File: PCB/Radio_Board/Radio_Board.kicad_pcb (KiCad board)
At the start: 2 copper layers, 1 part, among them J1 Conn_02x08_Counter_Clockwise

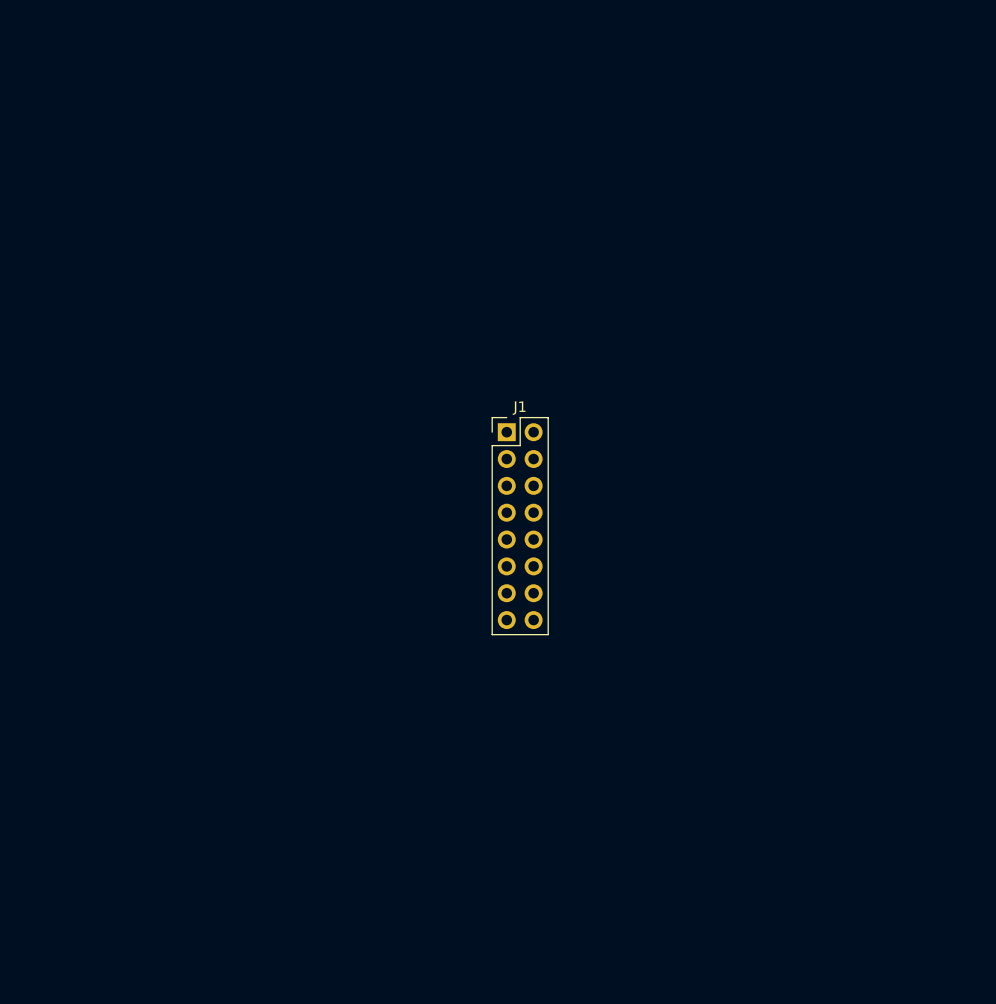
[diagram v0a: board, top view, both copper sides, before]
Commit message: added connector and started layout
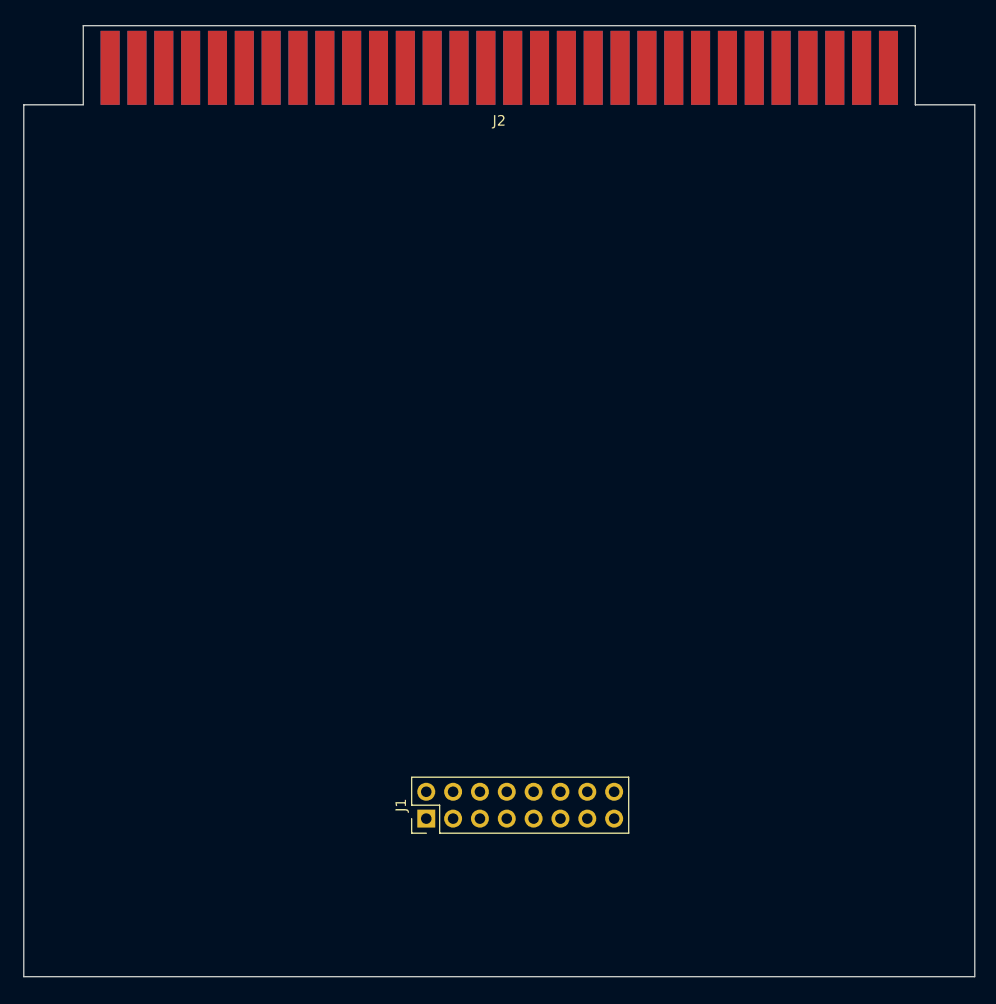
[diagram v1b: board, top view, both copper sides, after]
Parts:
- added J2: SE2-30, SE2-30:SE2-30, F.Cu at (148.8, 56.2)
- moved J1 37.4 mm to (141.8, 127.3), turned to 90 degrees
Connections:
- net /+5V renamed +5V
- net /GND renamed GND
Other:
- board outline added: 90 x 90 mm

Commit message: Wired Layout
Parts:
- removed J1: Conn_02x08_Counter_Clockwise, Connector_PinHeader_2.54mm:PinHeader_2x08_P2.54mm_Vertical
- added J3: Conn_02x08_Odd_Even, Connector_PinHeader_2.54mm:PinHeader_2x08_P2.54mm_Vertical, F.Cu at (140.6, 131.3)
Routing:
- net +5V: track 0.00 -> 125.9 mm, vias 0 -> 1
- net /Tx: track 0.00 -> 88.2 mm
- net /Rx: track 0.00 -> 81.6 mm
- added copper zone on B.Cu, net GND
- added copper zone on F.Cu, net GND

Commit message: small edits
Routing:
- net /Tx: track 88.2 -> 95.1 mm
- net +5V: track 125.9 -> 120.7 mm, vias 1 -> 5
- added copper zone on F.Cu, net +5V
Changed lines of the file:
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@@
 		(start 173 63)
 		(end 174 62)
-		(width 0.2)
-		(layer "F.Cu")
-		(net 1)
-	)
-	(segment
-		(start 174 62)
-		(end 175.5 60.5)
-		(width 0.2)
-		(layer "F.Cu")
-		(net 1)
-	)
-	(segment
-		(start 143.15 128.735)
-		(end 145.69 128.735)
-		(width 0.2)
-		(layer "F.Cu")
-		(net 1)
-	)
-	(segment
-		(start 175.5 60.5)
-		(end 175.42 60.42)
-		(width 0.2)
-		(layer "F.Cu")
-		(net 1)
-	)
-	(segment
-		(start 145.69 131.275)
-		(end 145.69 90.31)
-		(width 0.2)
+		(width 0.75)
+		(layer "F.Cu")
+		(net 1)
+	)
+	(segment
+		(start 175.42 60.58)
+		(end 174 62)
+		(width 0.75)
 		(layer "F.Cu")
 		(net 1)
@@
 		(start 170.34 60.34)
 		(end 173 63)
-		(width 0.2)
-		(layer "F.Cu")
-		(net 1)
-	)
-	(segment
-		(start 175.42 60.42)
-		(end 175.42 56.24)
-		(width 0.2)
+		(width 0.75)
+		(layer "F.Cu")
+		(net 1)
+	)
+	(segment
+		(start 173 63)
+		(end 145.69 90.31)
+		(width 0.75)
 		(layer "F.Cu")
 		(net 1)
@@
 		(start 172.88 60.88)
 		(end 174 62)
-		(width 0.2)
+		(width 0.75)
 		(layer "F.Cu")
 		(net 1)
@@
 		(start 172.88 56.24)
 		(end 172.88 60.88)
-		(width 0.2)
+		(width 0.75)
 		(layer "F.Cu")
 		(net 1)
@@
 		(start 170.34 56.24)
 		(end 170.34 60.34)
-		(width 0.2)
+		(width 0.75)
 		(layer "F.Cu")
 		(net 1)
@@
 	(segment
 		(start 145.69 90.31)
-		(end 173 63)
-		(width 0.2)
-		(layer "F.Cu")
-		(net 1)
-	)
-	(via
+		(end 145.69 128.735)
+		(width 0.75)
+		(layer "F.Cu")
+		(net 1)
+	)
+	(segment
+		(start 175.42 56.24)
+		(end 175.42 60.58)
+		(width 0.75)
+		(layer "F.Cu")
+		(net 1)
+	)
+	(via blind
+		(at 172.5 62.5)
+		(size 0.6)
+		(drill 0.3)
+		(layers "F.Cu" "B.Cu")
+		(net 1)
+	)
+	(via blind
+		(at 174.5 61.5)
+		(size 0.6)
+		(drill 0.3)
+		(layers "F.Cu" "B.Cu")
+		(net 1)
+	)
+	(via blind
+		(at 174 62)
+		(size 0.6)
+		(drill 0.3)
+		(layers "F.Cu" "B.Cu")
+		(net 1)
+	)
+	(via blind
+		(at 173.5 62.5)
+		(size 0.6)
+		(drill 0.3)
+		(layers "F.Cu" "B.Cu")
+		(net 1)
+	)
+	(via blind
 		(at 173 63)
 		(size 0.6)
@@
 		(start 174 62)
 		(end 173 63)
-		(width 0.2)
+		(width 0.75)
 		(layer "B.Cu")
 		(net 1)
@@
 		(start 175.42 60.58)
 		(end 175.42 56.24)
-		(width 0.2)
+		(width 0.75)
 		(layer "B.Cu")
 		(net 1)
@@
 		(start 170.34 60.34)
 		(end 173 63)
-		(width 0.2)
+		(width 0.75)
 		(layer "B.Cu")
 		(net 1)
@@
 		(start 170.34 56.24)
 		(end 170.34 60.34)
-		(width 0.2)
+		(width 0.75)
 		(layer "B.Cu")
 		(net 1)
@@
 		(start 172.88 56.24)
 		(end 172.88 60.88)
-		(width 0.2)
+		(width 0.75)
 		(layer "B.Cu")
 		(net 1)
@@
 		(start 172.88 60.88)
 		(end 174 62)
-		(width 0.2)
+		(width 0.75)
 		(layer "B.Cu")
 		(net 1)
@@
 		(start 174 62)
 		(end 175.42 60.58)
-		(width 0.2)
-		(layer "B.Cu")
-		(net 1)
-	)
-	(segment
-		(start 144.301 131.51376)
-		(end 144.301 130.56024)
-		(width 0.2)
-		(layer "F.Cu")
-		(net 3)
+		(width 0.75)
+		(layer "B.Cu")
+		(net 1)
 	)
 	(segment
 		(start 150.77 131.275)
-		(end 149.619 132.426)
-		(width 0.2)
-		(layer "F.Cu")
-		(net 3)
-	)
-	(segment
-		(start 132.24 58.84)
+		(end 148.045 134)
+		(width 0.2)
+		(layer "F.Cu")
+		(net 3)
+	)
+	(segment
+		(start 132.24 129.99)
 		(end 132.24 56.24)
 		(width 0.2)
@@
 	)
 	(segment
-		(start 142.67324 129.886)
-		(end 141.999 129.21176)
-		(width 0.2)
-		(layer "F.Cu")
-		(net 3)
-	)
-	(segment
-		(start 141.999 68.599)
-		(end 132.24 58.84)
-		(width 0.2)
-		(layer "F.Cu")
-		(net 3)
-	)
-	(segment
-		(start 145.21324 132.426)
-		(end 144.301 131.51376)
-		(width 0.2)
-		(layer "F.Cu")
-		(net 3)
-	)
-	(segment
-		(start 143.62676 129.886)
-		(end 142.67324 129.886)
-		(width 0.2)
-		(layer "F.Cu")
-		(net 3)
-	)
-	(segment
-		(start 141.999 129.21176)
-		(end 141.999 68.599)
-		(width 0.2)
-		(layer "F.Cu")
-		(net 3)
-	)
-	(segment
-		(start 149.619 132.426)
-		(end 145.21324 132.426)
-		(width 0.2)
-		(layer "F.Cu")
-		(net 3)
-	)
-	(segment
-		(start 144.301 130.56024)
-		(end 143.62676 129.886)
+		(start 136.25 134)
+		(end 132.24 129.99)
+		(width 0.2)
+		(layer "F.Cu")
+		(net 3)
+	)
+	(segment
+		(start 148.045 134)
+		(end 136.25 134)
 		(width 0.2)
 		(layer "F.Cu")
@@
 	)
 	(zone
+		(net 1)
+		(net_name "+5V")
+		(layer "F.Cu")
+		(hatch edge 0.5)
+		(priority 1)
+		(connect_pads yes
+			(clearance 0.5)
+		)
+		(min_thickness 0.25)
+		(filled_areas_thickness no)
+		(fill yes
+			(thermal_gap 0.5)
+			(thermal_bridge_width 0.5)
+		)
+		(polygon
+			(pts
+				(xy 142 127.5) (xy 142 130) (xy 144.5 130) (xy 144.5 132.5) (xy 147 132.5) (xy 147 127.5)
+			)
+		)
+	)
+	(zone

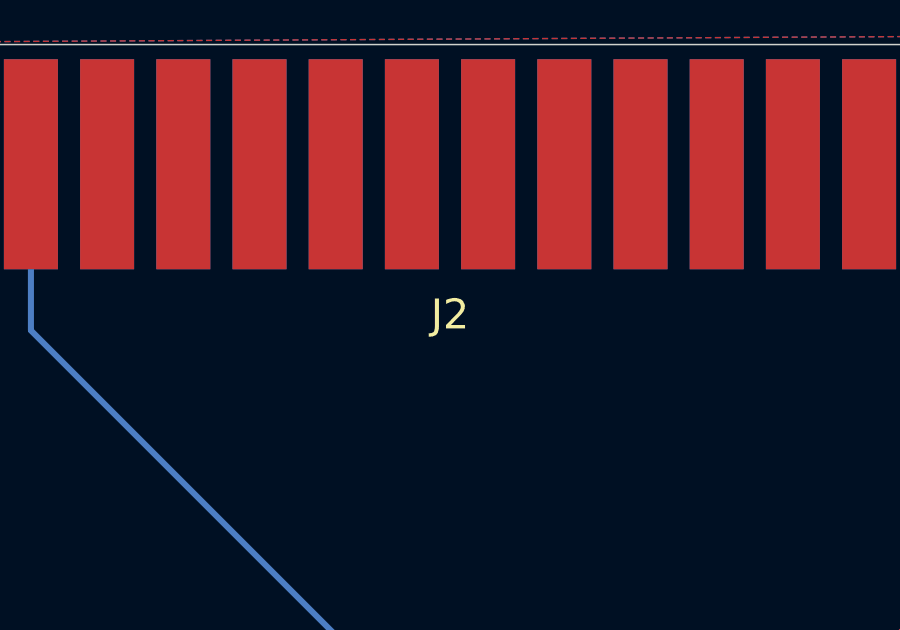
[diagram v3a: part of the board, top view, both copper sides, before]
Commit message: updated footprint from lib
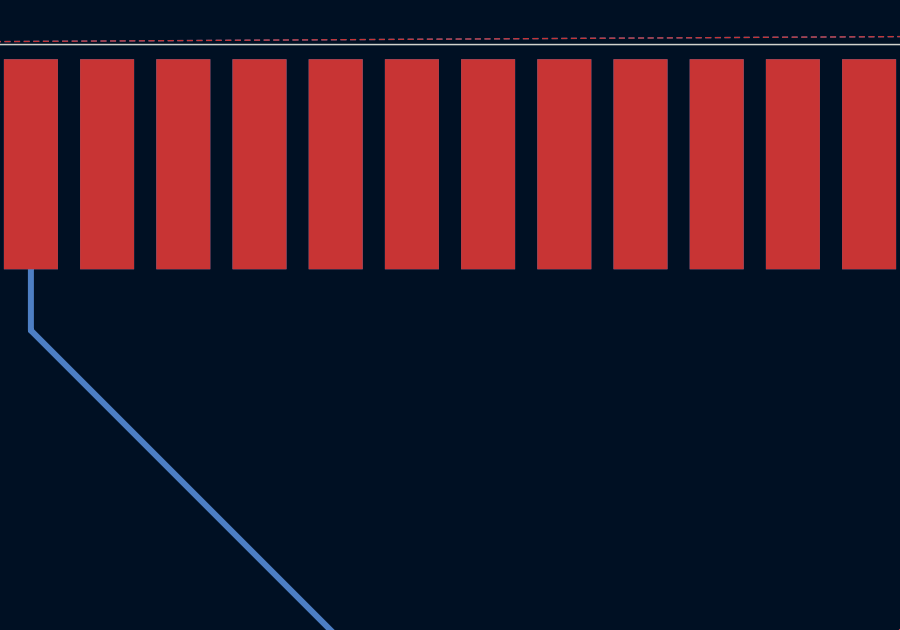
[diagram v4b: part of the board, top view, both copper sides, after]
